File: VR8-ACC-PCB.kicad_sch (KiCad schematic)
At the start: 41 parts, among them IC1 LM393P, IC2 VO14642AT, IC3 VO14642AT, IC4 KT12-1A-40L-THT, IC5 NE555P, Q1 Q_NMOS_Depletion_GDS, Q2 Q_NMOS_Depletion_GDS, Q3 Q_NMOS_Depletion_GDS

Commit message: J4 reorientation
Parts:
- renumbered D11 to D10, D10 to D11
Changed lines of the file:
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@@
 		(on_board yes)
 		(dnp no)
-		(property "Reference" "D10"
+		(property "Reference" "D11"
 			(at 196.85 125.7299 90)
 			(effects
@@
 			(project "Acc PCB"
 				(path "/351a0cd1-2107-41e5-ac44-a6aef25d291e"
-					(reference "D10")
+					(reference "D11")
 					(unit 1)
 				)
@@
 		(on_board yes)
 		(dnp no)
-		(property "Reference" "D11"
+		(property "Reference" "D10"
 			(at 53.34 39.3699 90)
 			(effects
@@
 			(project ""
 				(path "/351a0cd1-2107-41e5-ac44-a6aef25d291e"
-					(reference "D11")
+					(reference "D10")
 					(unit 1)
 				)

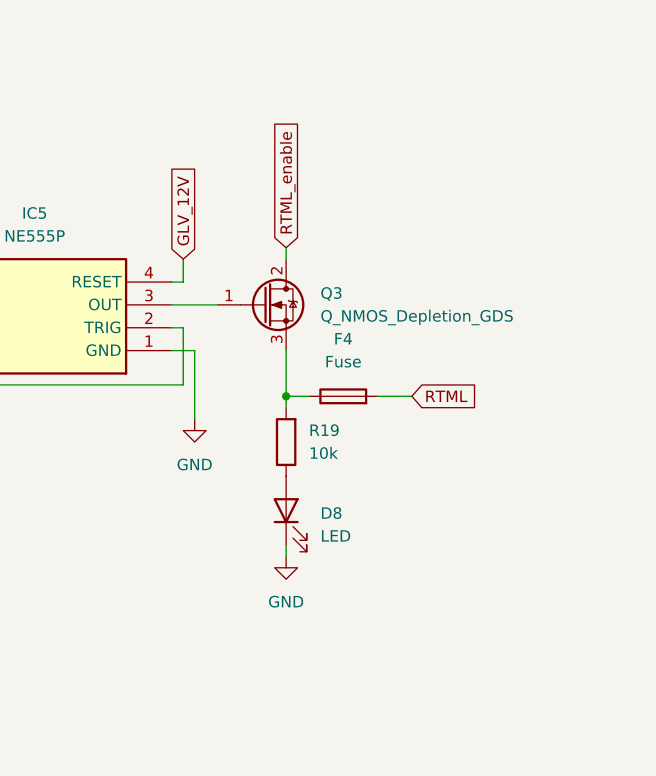
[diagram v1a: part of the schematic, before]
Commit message: add ne555 output resister
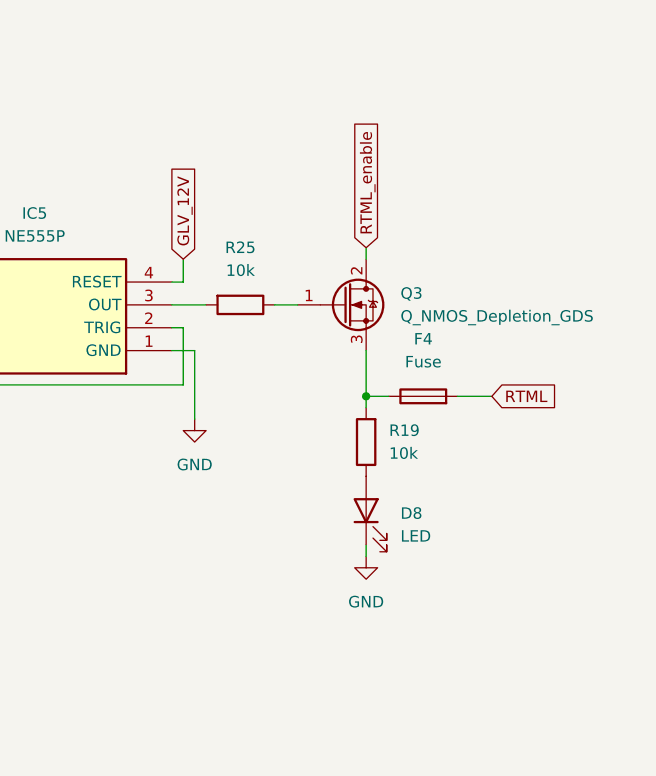
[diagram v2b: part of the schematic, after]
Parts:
- added R25: 10k, Resistor_SMD:R_1206_3216Metric_Pad1.30x1.75mm_HandSolder, symbol Device:R
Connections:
- net at IC5.3 (OUT): now also R25.2; no longer Q3.1 (G)
- new net: Q3.1 (G), R25.1
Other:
- moved on the sheet: D8, F4, Q3, R19

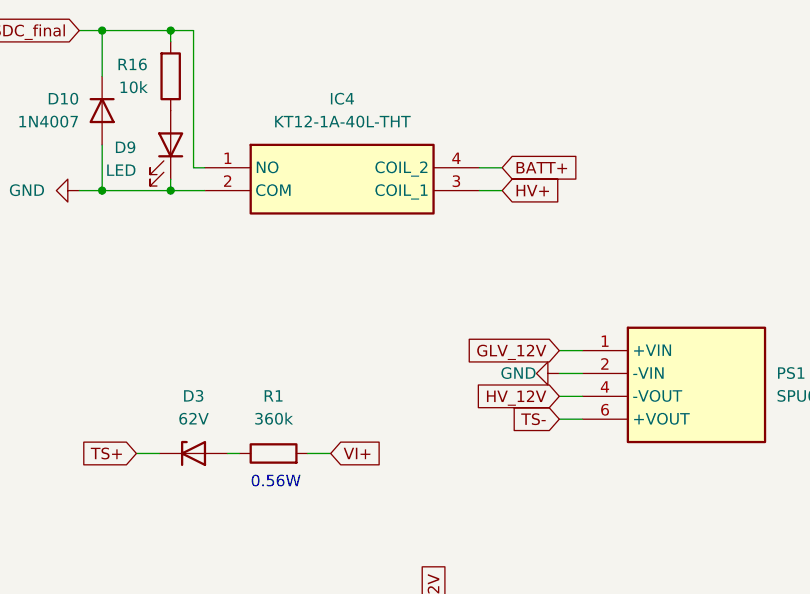
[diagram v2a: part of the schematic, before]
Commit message: fix wrong DCDC & precharge relay pin connection
swap out +/out - of the DCDC
swap coil/contact of the relay
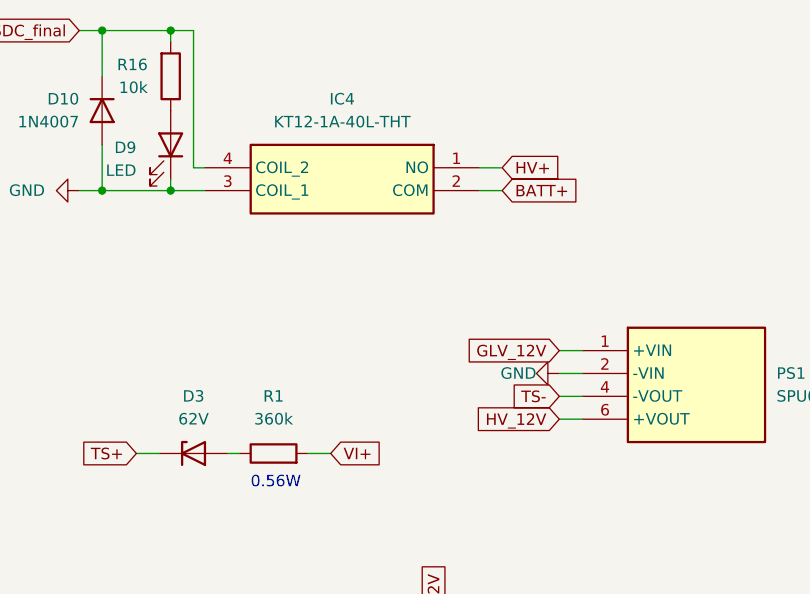
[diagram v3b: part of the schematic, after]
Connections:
- net BATT+: now also IC4.2 (COM); no longer IC4.4 (COIL_2)
- net GND: now also IC4.3 (COIL_1); no longer IC4.2 (COM)
- net HV+: now also IC4.1 (NO); no longer IC4.3 (COIL_1)
- net HV_12V: now also PS1.6 (+VOUT); no longer PS1.4 (-VOUT)
- net SDC_final: now also IC4.4 (COIL_2); no longer IC4.1 (NO)
- net TS-: now also PS1.4 (-VOUT); no longer PS1.6 (+VOUT)
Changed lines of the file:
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@@
 	(wire
 		(pts
-			(xy 100.33 46.99) (xy 97.79 46.99)
+			(xy 100.33 49.53) (xy 97.79 49.53)
 		)
 		(stroke
@@
 	(wire
 		(pts
-			(xy 97.79 49.53) (xy 100.33 49.53)
+			(xy 97.79 46.99) (xy 100.33 46.99)
 		)
 		(stroke
@@
 	(global_label "BATT+"
 		(shape input)
-		(at 100.33 46.99 0)
+		(at 100.33 49.53 0)
 		(fields_autoplaced yes)
 		(effects
@@
 		)
 		(property "Intersheetrefs" "${INTERSHEET_REFS}"
-			(at 109.1814 46.99 0)
+			(at 109.1814 49.53 0)
 			(effects
 				(font
@@
 	(global_label "TS-"
 		(shape input)
-		(at 106.68 74.93 180)
+		(at 106.68 72.39 180)
 		(fields_autoplaced yes)
 		(effects
@@
 		)
 		(property "Intersheetrefs" "${INTERSHEET_REFS}"
-			(at 99.9453 74.93 0)
+			(at 99.9453 72.39 0)
 			(effects
 				(font
@@
 	(global_label "HV+"
 		(shape input)
-		(at 100.33 49.53 0)
+		(at 100.33 46.99 0)
 		(fields_autoplaced yes)
 		(effects
@@
 		)
 		(property "Intersheetrefs" "${INTERSHEET_REFS}"
-			(at 107.3067 49.53 0)
+			(at 107.3067 46.99 0)
 			(effects
 				(font
@@
 	(global_label "HV_12V"
 		(shape input)
-		(at 106.68 72.39 180)
+		(at 106.68 74.93 180)
 		(fields_autoplaced yes)
 		(effects
@@
 		)
 		(property "Intersheetrefs" "${INTERSHEET_REFS}"
-			(at 96.8005 72.39 0)
+			(at 96.8005 74.93 0)
 			(effects
 				(font
@@
 	(symbol
 		(lib_id "Samacsys:KT12-1A-40L-THT")
-		(at 67.31 46.99 0)
+		(at 97.79 46.99 0)
+		(mirror y)
 		(unit 1)
 		(exclude_from_sim no)
@@
 		(on_board yes)
 		(dnp no)
-		(fields_autoplaced yes)
 		(property "Reference" "IC4"
 			(at 82.55 39.37 0)
@@
 		)
 		(property "Footprint" "Samacsys:KT121A40LTHT"
-			(at 93.98 141.91 0)
+			(at 71.12 141.91 0)
 			(effects
 				(font
@@
 		)
 		(property "Datasheet" "https://standexelectronics.com/resources/technical-library/technical-papers/datasheet-kt-series-reed-relay/"
-			(at 93.98 241.91 0)
+			(at 71.12 241.91 0)
 			(effects
 				(font
@@
 		)
 		(property "Description" "Reed Relays 1 Form A SPST-NO 12V THT High IR"
-			(at 67.31 46.99 0)
+			(at 97.79 46.99 0)
 			(effects
 				(font
@@
 		)
 		(property "Height" "8.7"
-			(at 93.98 441.91 0)
+			(at 71.12 441.91 0)
 			(effects
 				(font
@@
 		)
 		(property "Mouser Part Number" "876-KT12-1A-40L-THT"
-			(at 93.98 541.91 0)
+			(at 71.12 541.91 0)
 			(effects
 				(font
@@
 		)
 		(property "Mouser Price/Stock" ""
-			(at 93.98 641.91 0)
+			(at 71.12 641.91 0)
 			(effects
 				(font
@@
 		)
 		(property "Manufacturer_Name" "STANDEXMEDER"
-			(at 93.98 741.91 0)
+			(at 71.12 741.91 0)
 			(effects
 				(font
@@
 		)
 		(property "Manufacturer_Part_Number" "KT12-1A-40L-THT"
-			(at 93.98 841.91 0)
+			(at 71.12 841.91 0)
 			(effects
 				(font
@@
 		)
 		(property "Sim.Device" "SW"
-			(at 67.31 46.99 0)
+			(at 97.79 46.99 0)
 			(effects
 				(font
@@
 		)
 		(property "Sim.Type" "V"
-			(at 67.31 46.99 0)
+			(at 97.79 46.99 0)
 			(effects
 				(font
@@
 		)
 		(property "Sim.Pins" "1=ctrl+ 2=ctrl- 3=no+ 4=no-"
-			(at 67.31 46.99 0)
+			(at 97.79 46.99 0)
 			(effects
 				(font
@@
 		)
 		(property "Sim.Params" "thr=8.4 his=1.4 ron=150m"
-			(at 67.31 46.99 0)
+			(at 97.79 46.99 0)
 			(effects
 				(font
@@
 		)
 		(property "Availability" ""
-			(at 67.31 46.99 0)
+			(at 97.79 46.99 0)
 			(effects
 				(font
@@
 		)
 		(property "Check_prices" ""
-			(at 67.31 46.99 0)
+			(at 97.79 46.99 0)
 			(effects
 				(font
@@
 		)
 		(property "Description_1" ""
-			(at 67.31 46.99 0)
+			(at 97.79 46.99 0)
 			(effects
 				(font
@@
 		)
 		(property "Field5" ""
-			(at 67.31 46.99 0)
+			(at 97.79 46.99 0)
 			(effects
 				(font
@@
 		)
 		(property "MANUFACTURER" ""
-			(at 67.31 46.99 0)
+			(at 97.79 46.99 0)
 			(effects
 				(font
@@
 		)
 		(property "MAXIMUM_PACKAGE_HEIGHT" ""
-			(at 67.31 46.99 0)
+			(at 97.79 46.99 0)
 			(effects
 				(font
@@
 		)
 		(property "MF" ""
-			(at 67.31 46.99 0)
+			(at 97.79 46.99 0)
 			(effects
 				(font
@@
 		)
 		(property "MP" ""
-			(at 67.31 46.99 0)
+			(at 97.79 46.99 0)
 			(effects
 				(font
@@
 		)
 		(property "PARTREV" ""
-			(at 67.31 46.99 0)
+			(at 97.79 46.99 0)
 			(effects
 				(font
@@
 		)
 		(property "Package" ""
-			(at 67.31 46.99 0)
+			(at 97.79 46.99 0)
 			(effects
 				(font
@@
 		)
 		(property "Price" ""
-			(at 67.31 46.99 0)
+			(at 97.79 46.99 0)
 			(effects
 				(font
@@
 		)
 		(property "STANDARD" ""
-			(at 67.31 46.99 0)
+			(at 97.79 46.99 0)
 			(effects
 				(font
@@
 		)
 		(property "SnapEDA_Link" ""
-			(at 67.31 46.99 0)
+			(at 97.79 46.99 0)
 			(effects
 				(font

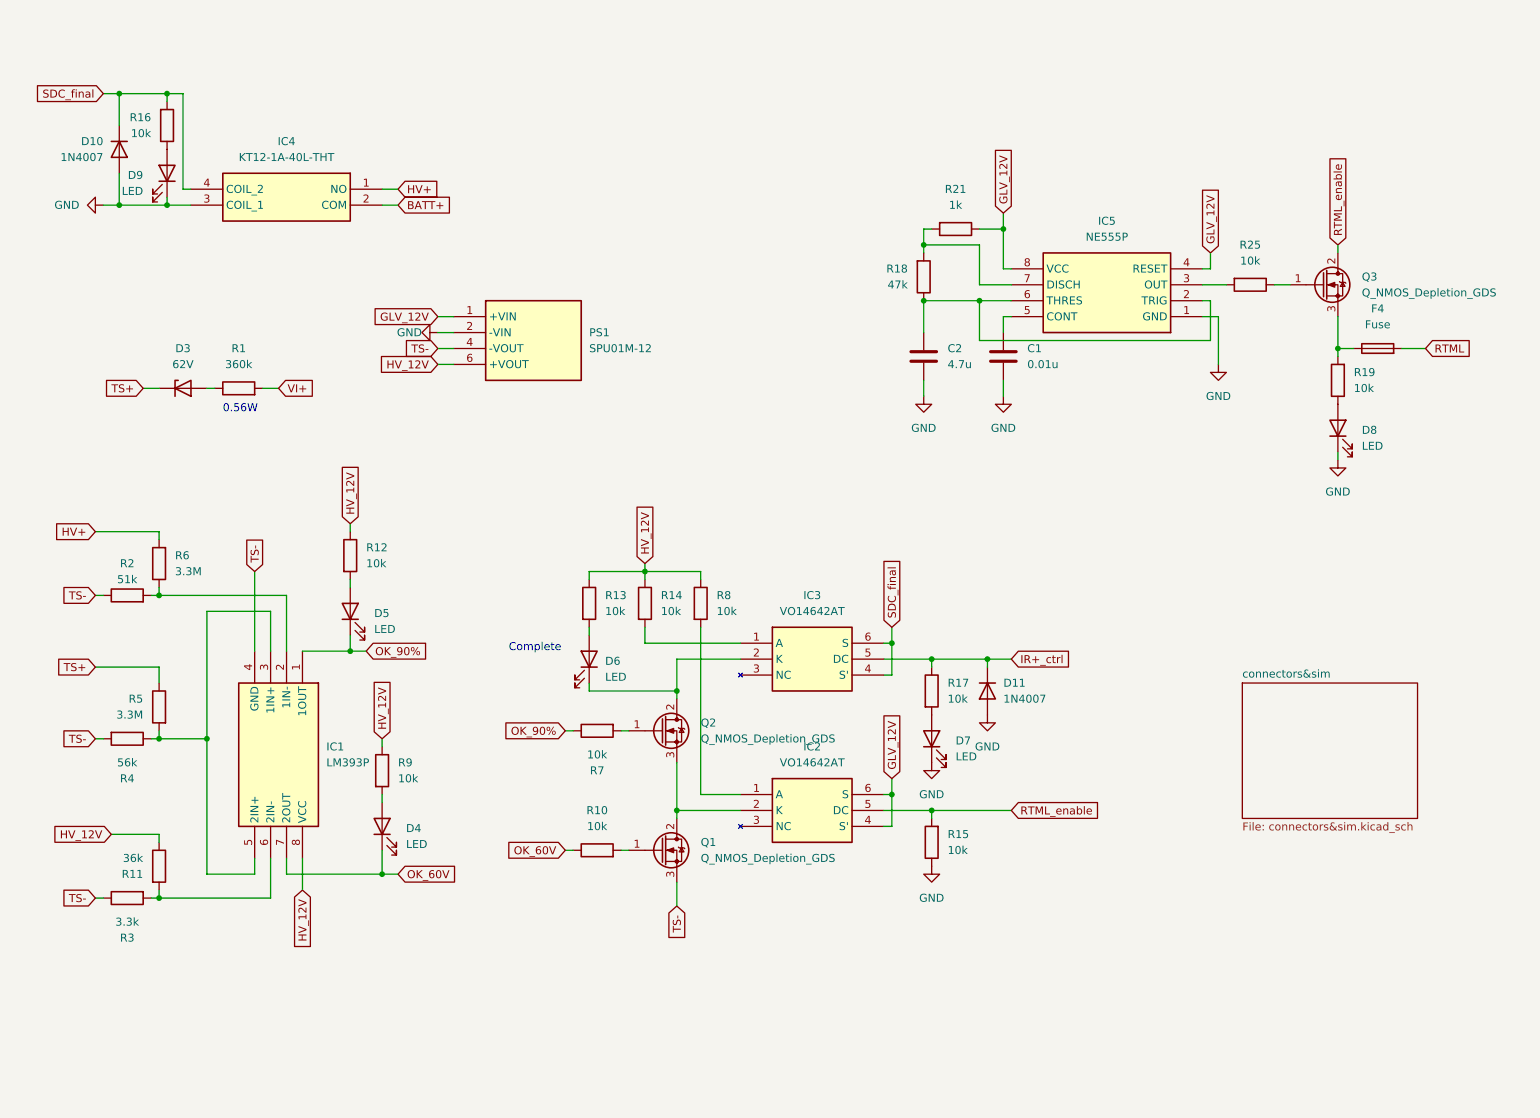
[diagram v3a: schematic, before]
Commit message: find and fix test errors, some improvement
1. remove onboard fuse (now is inline)
2. change RTML nmos to pmos (to make nmos on, RTML only have V_G-V_th=10V, which is not enough to drive RTML)
3. new voltage divider config (resistors tolerance is matter, <1% is better)
4. add IR+_ctrl signal output to J5
5. J7 is now used for powering Arduino rather than bridging interlock signal (SDC_after_MSD is removed from J5 as well)
6. explain the working principle on sch
7. move to kicad 10
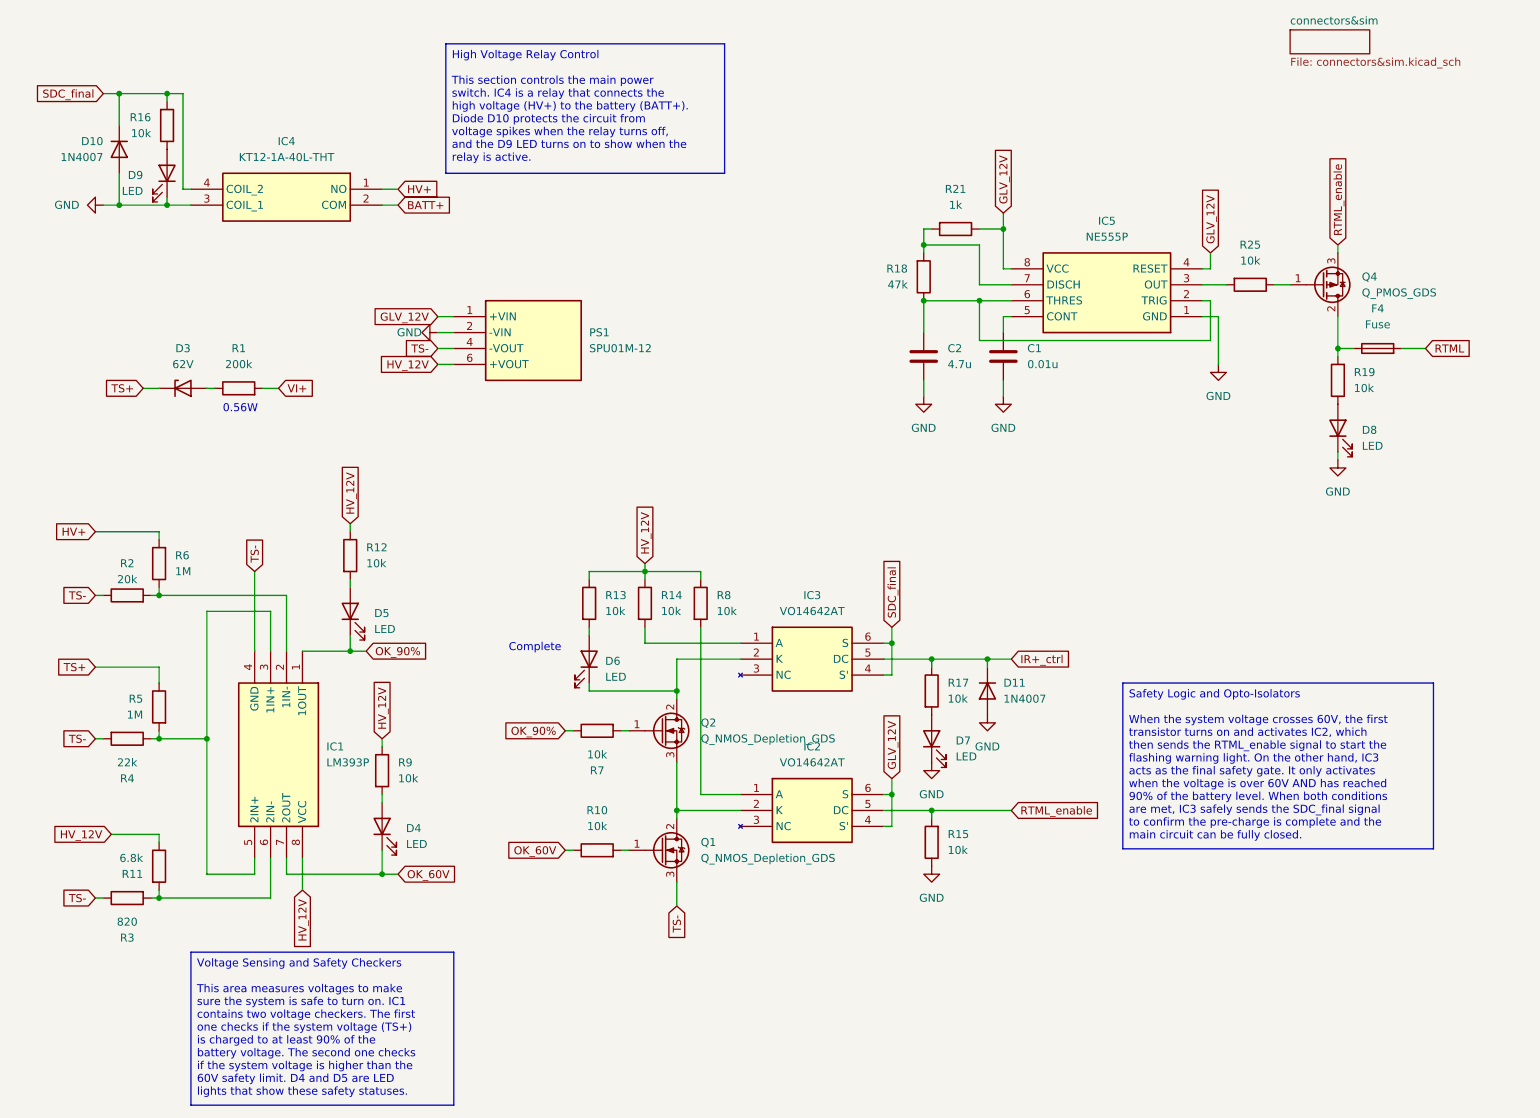
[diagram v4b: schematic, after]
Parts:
- removed Q3: Q_NMOS_Depletion_GDS, Package_TO_SOT_THT:TO-251-3_Vertical, symbol Transistor_FET_Other:Q_NMOS_Depletion_GDS
- added Q4: Q_PMOS_GDS, Package_TO_SOT_THT:TO-220-3_Vertical, symbol Transistor_FET:Q_PMOS_GDS
- R1: value 360k -> 200k
- R11: value 36k -> 6.8k
- R2: value 51k -> 20k
- R3: value 3.3k -> 820
- R4: value 56k -> 22k
- R5, R6: value 3.3M -> 1M
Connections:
- net RTML_enable: now also Q4.3 (S)
- net at F4.1, R19.2: now also Q4.2 (D)
- net at R25.1: now also Q4.1 (G)
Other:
- title: VR8-Acc-PCB -> VR8-TBC-PCB
